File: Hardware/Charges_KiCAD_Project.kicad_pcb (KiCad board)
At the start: 4 copper layers, 80 x 93.2 mm, 81 parts, among them J1 Terminal Block, J2 Terminal Block, J3 DB37_Male_MountingHoles, J4 10118192-0001LF, Q1 SI7232DN-T1-GE3, Q2 SI7232DN-T1-GE3, SW1 MCU Reset, U1 MS5607-02BA, U2 STM32L562VET6Q, U3 LP38692MPX-ADJ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

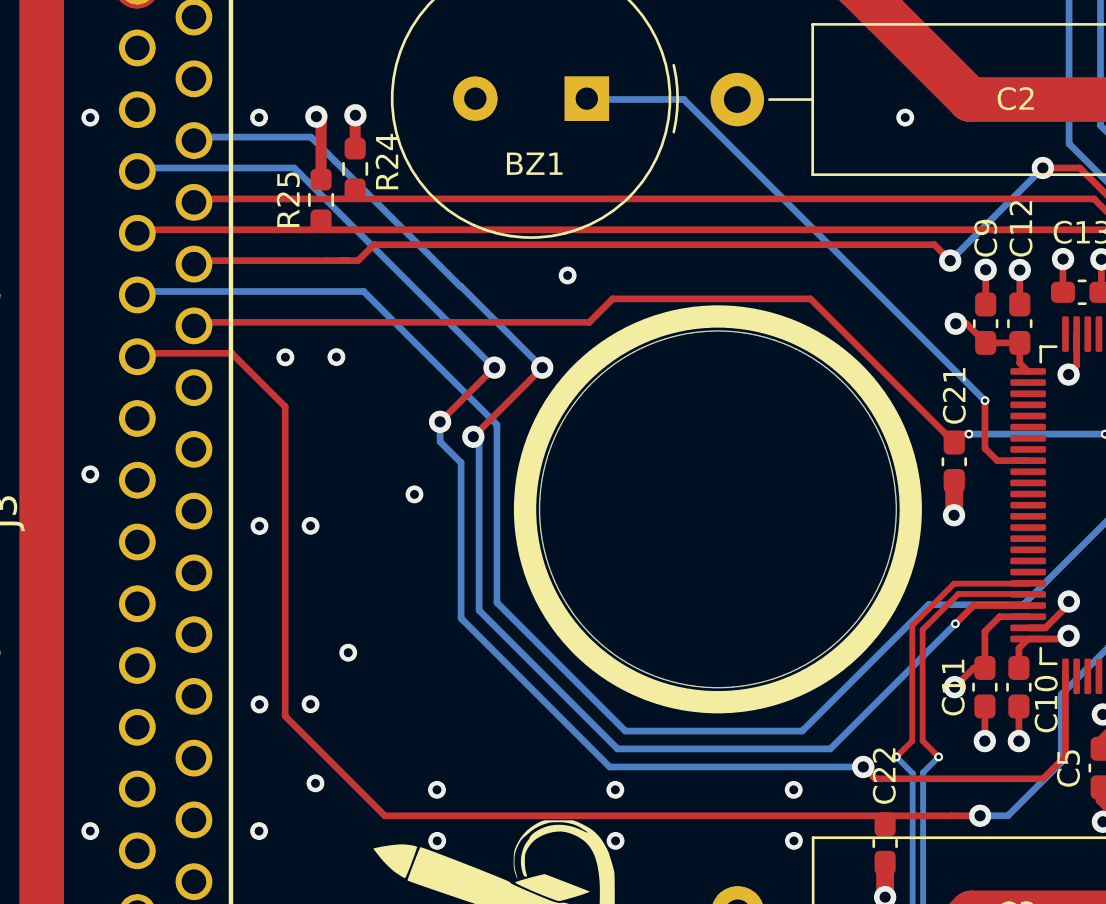
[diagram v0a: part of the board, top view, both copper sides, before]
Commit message: Moved center hole to the left by 2 mm.
someone made an opsie and forgot that the dsub was WIDE. moved the center hole and a few traces over. remade two traces to eliminate right angles.
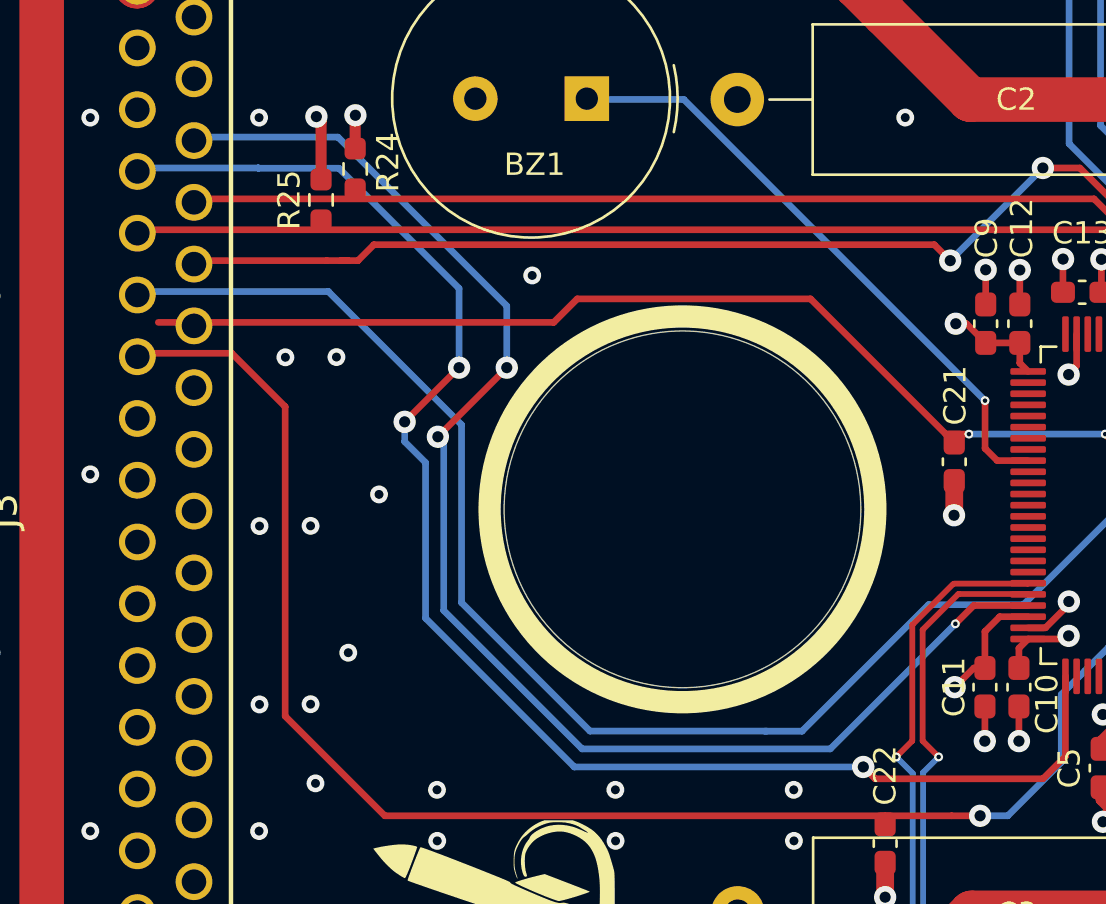
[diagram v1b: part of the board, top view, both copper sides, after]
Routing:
- net /37 Pin DSUB/SWCLK: track 66.5 -> 68.6 mm
- net /37 Pin DSUB/SWDIO: track 61.6 -> 63.3 mm
- net /37 Pin DSUB/Fire: track 57.9 -> 59.5 mm
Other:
- outline, holes or cut-outs redrawn
